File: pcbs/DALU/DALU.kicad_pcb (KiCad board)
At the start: 4 copper layers, 94 parts, among them J201 Conn_02x20_Odd_Even, U201 74HC245, U202 74HC245, U203 74HC245, U301 74HC138, U401 74HC86, U402 74HC08, U403 74HC86, U404 74HC86, U405 74HC283, U406 74HC283, U407 74HC245, U408 74HC245, U501 74HC00, U502 74HC00, U503 74HC245, U601 74HC86, U602 74HC86, U603 74HC245, U701 74HC32, U702 74HC32, U703 74HC245, U801 74HC74, U802 74HC32, U803 74HCT574, U901 74HC08, U902 74HC08, U903 74HC245

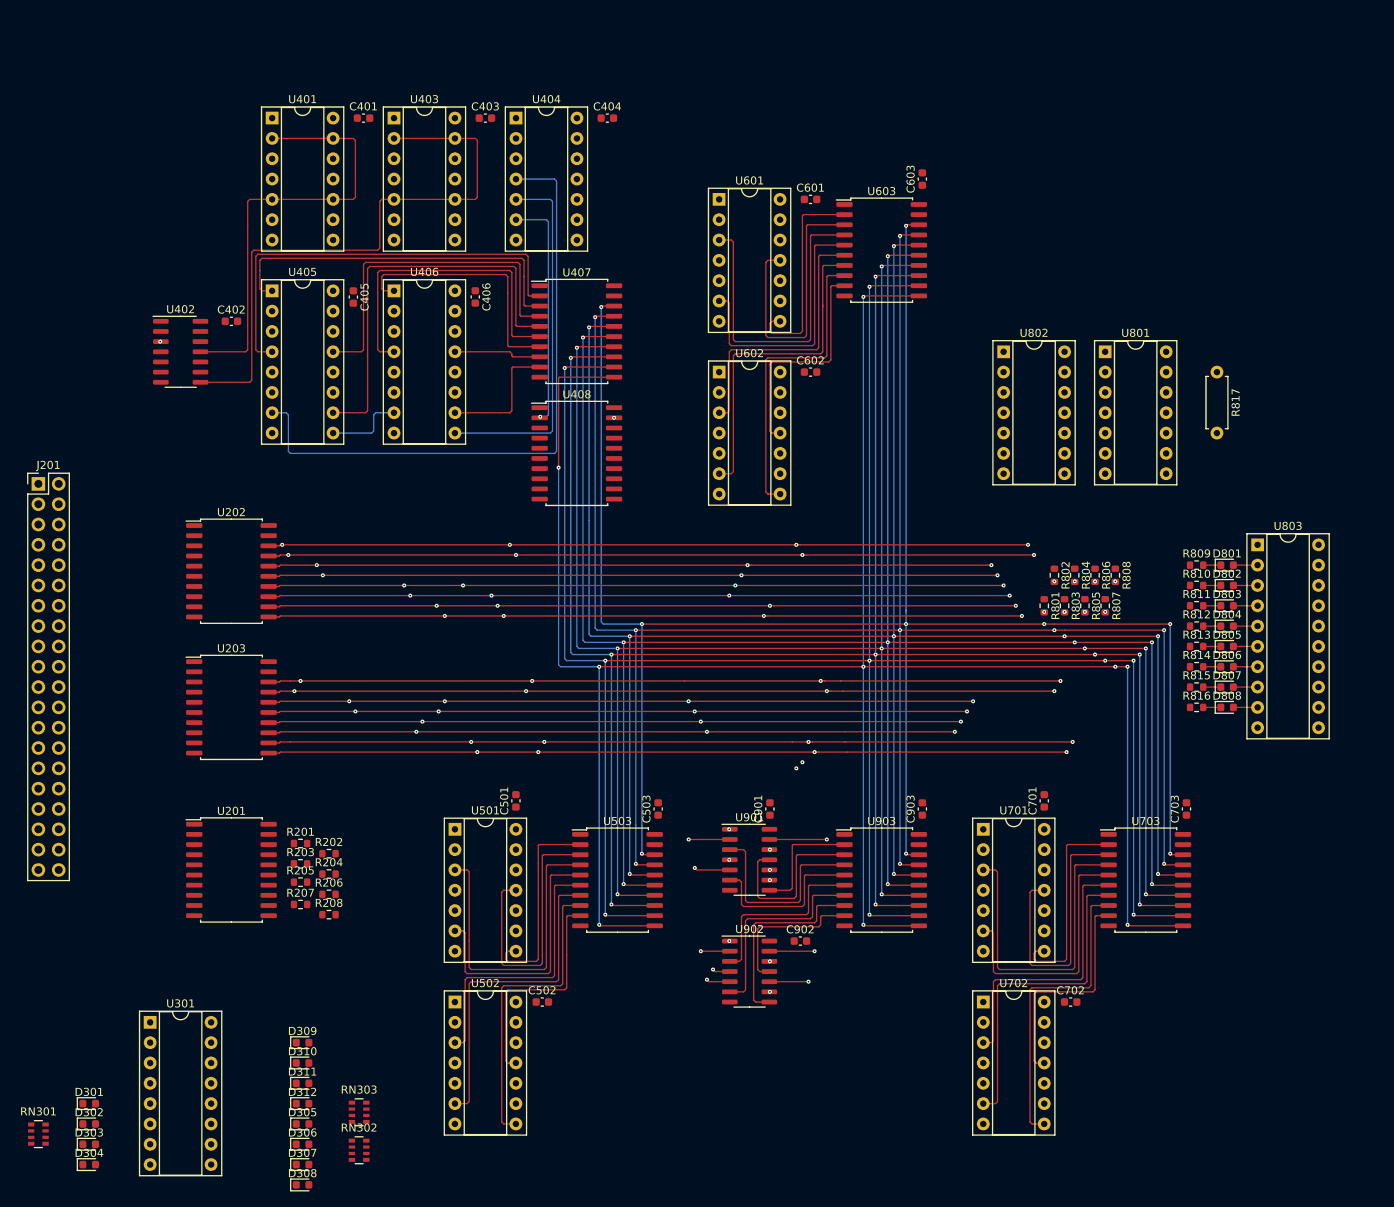
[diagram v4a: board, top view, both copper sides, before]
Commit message: Starting to connect up control wires
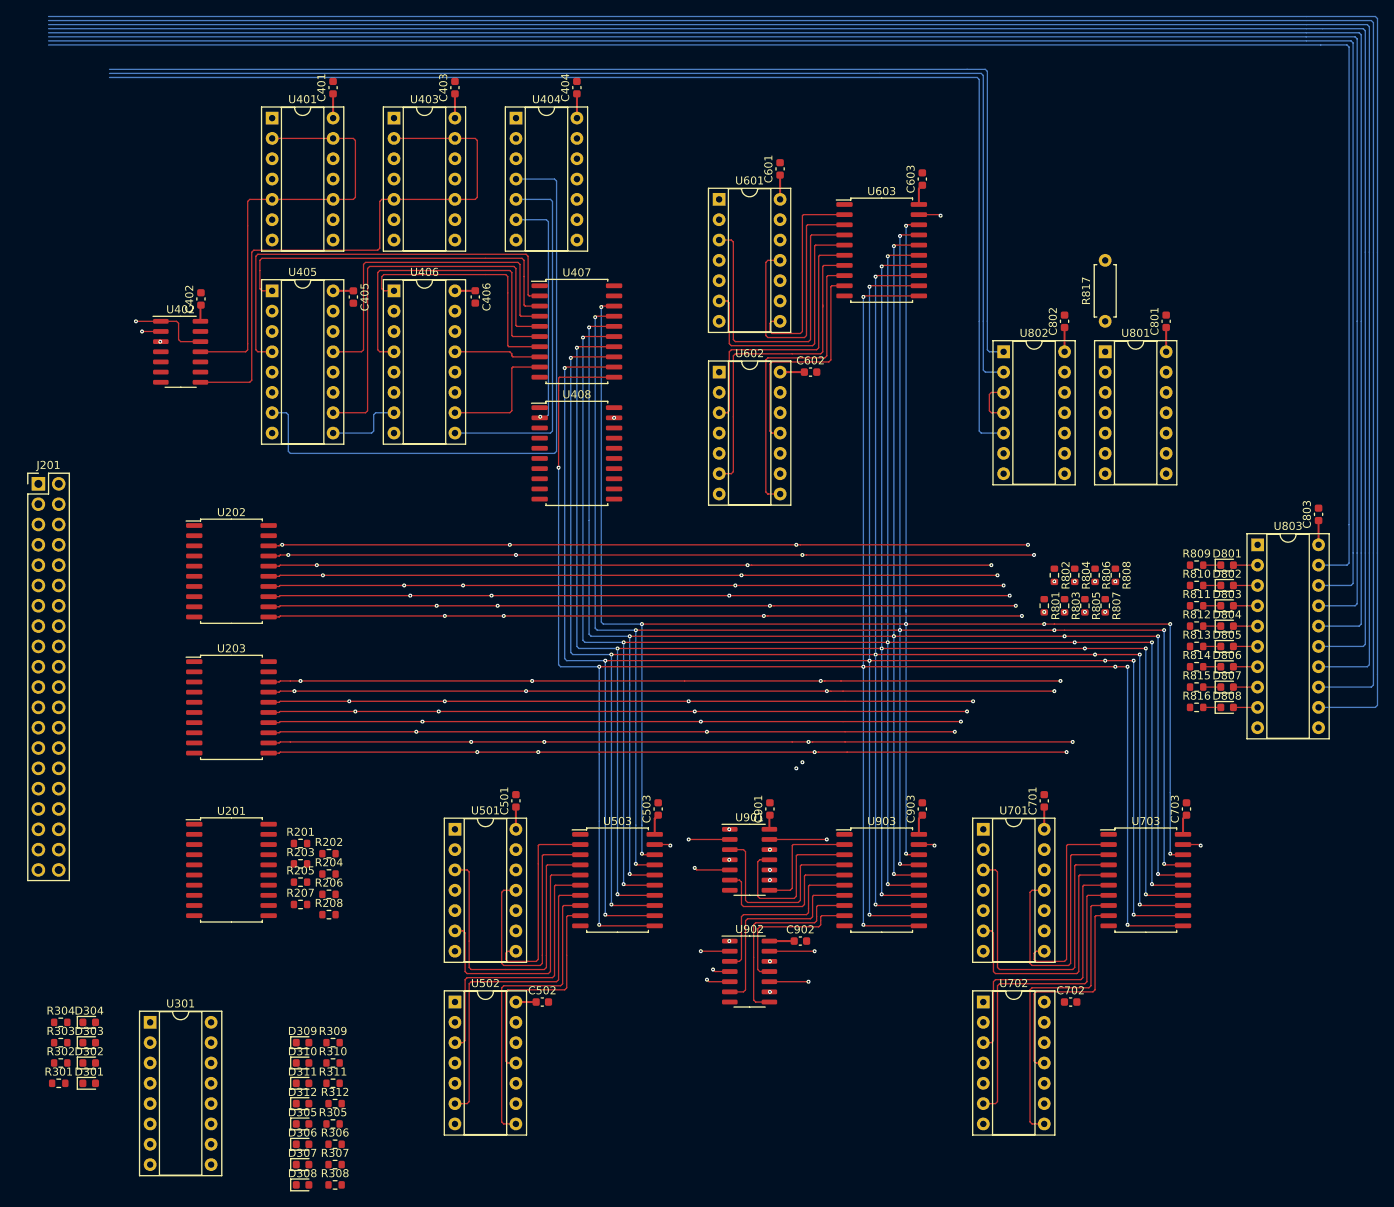
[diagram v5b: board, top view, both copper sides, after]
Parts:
- removed RN301, RN302, RN303: 4k7, Resistor_SMD:R_Array_Convex_4x0603
- added C801: 100n, Capacitor_SMD:C_0603_1608Metric, F.Cu at (175.3, 78.7)
- added C802: 100n, Capacitor_SMD:C_0603_1608Metric, F.Cu at (162.6, 78.7)
- added C803: 100n, Capacitor_SMD:C_0603_1608Metric, F.Cu at (194.3, 102.9)
- added R301: 4k7, Resistor_SMD:R_0603_1608Metric, F.Cu at (36.8, 174.0)
- added R302: 4k7, Resistor_SMD:R_0603_1608Metric, F.Cu at (37.1, 171.4)
- added R303: 4k7, Resistor_SMD:R_0603_1608Metric, F.Cu at (37.1, 168.9)
- added R304: 4k7, Resistor_SMD:R_0603_1608Metric, F.Cu at (37.1, 166.4)
- added R305: 4k7, Resistor_SMD:R_0603_1608Metric, F.Cu at (71.1, 179.1)
- added R306: 4k7, Resistor_SMD:R_0603_1608Metric, F.Cu at (71.4, 181.6)
- added R307: 4k7, Resistor_SMD:R_0603_1608Metric, F.Cu at (71.4, 184.2)
- added R308: 4k7, Resistor_SMD:R_0603_1608Metric, F.Cu at (71.4, 186.7)
- added R309: 4k7, Resistor_SMD:R_0603_1608Metric, F.Cu at (71.1, 168.9)
- added R310: 4k7, Resistor_SMD:R_0603_1608Metric, F.Cu at (71.1, 171.4)
- added R311: 4k7, Resistor_SMD:R_0603_1608Metric, F.Cu at (71.1, 174.0)
- added R312: 4k7, Resistor_SMD:R_0603_1608Metric, F.Cu at (71.4, 176.5)
- moved D304 17.8 mm to (40.6, 166.4)
- moved R817 15.3 mm to (167.6, 78.7), turned to 90 degrees
- moved D303 12.7 mm to (40.6, 168.9)
- moved D302 7.62 mm to (40.6, 171.4)
- moved C401 5.39 mm to (71.1, 49.5), turned to 90 degrees
- moved C403 5.39 mm to (86.4, 49.5), turned to 90 degrees
- moved C404 5.39 mm to (101.6, 49.5), turned to 90 degrees
- moved C601 5.39 mm to (127.0, 59.7), turned to 90 degrees
- moved C402 4.72 mm to (54.6, 75.9), turned to 90 degrees
- moved D301 2.54 mm to (40.6, 174.0)
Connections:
- U402 pad 1: /AdderSubtractor/~{ADD} -> /Decoder/~{ADD}
- U402 pad 12: /AdderSubtractor/~{ADD} -> /Decoder/~{ADD}
- U402 pad 2: /AdderSubtractor/~{SUBTRACT} -> /Decoder/~{SUBTRACT}
- U402 pad 9: /AdderSubtractor/~{ADD} -> /Decoder/~{ADD}
- U404 pad 4: /AdderSubtractor/~{ADD} -> /Decoder/~{ADD}
- U405 pad 7: /AdderSubtractor/~{ADD} -> /Decoder/~{ADD}
- U503 pad 19: /NAND/~{NAND} -> /Decoder/~{NAND}
- U603 pad 19: unconnected-(U603-Pad19) -> /Decoder/~{XOR}
- U703 pad 19: /OR/~{OR} -> /Decoder/~{OR}
- U802 pad 14: unconnected-(U802-Pad14) -> +5V
- U802 pad 7: unconnected-(U802-Pad7) -> GND
- U903 pad 19: /AND/~{AND} -> /Decoder/~{AND}
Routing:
- net /Output Stage/C7: track 0.00 -> 259.5 mm
- net /Output Stage/C6: track 0.00 -> 255.5 mm
- net /Output Stage/C5: track 0.00 -> 251.4 mm
- net /Output Stage/C4: track 0.00 -> 247.4 mm
- net /Output Stage/EXECUTE: track 0.00 -> 243.5 mm
- net /Output Stage/C3: track 0.00 -> 243.3 mm
- net /Output Stage/C2: track 0.00 -> 239.2 mm
- net /Output Stage/C1: track 0.00 -> 235.2 mm
- net /Output Stage/C0: track 0.00 -> 231.1 mm
- net /Decoder/~{XOR}: track 0.00 -> 221.8 mm, vias 0 -> 1
- net /Decoder/~{ADD}: track 0.00 -> 187.3 mm, vias 0 -> 1
- net /Decoder/~{OR}: track 0.00 -> 173.5 mm, vias 0 -> 1
- net /Output Stage/COMMIT: track 0.00 -> 155.9 mm
- net /Output Stage/DECODE: track 0.00 -> 146.8 mm
- net /Decoder/~{AND}: track 0.00 -> 143.3 mm, vias 0 -> 1
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
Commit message: Finish preliminary routing
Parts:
- added C201: 100n, Capacitor_SMD:C_0603_1608Metric, F.Cu at (66.3, 139.2)
- added C202: 100n, Capacitor_SMD:C_0603_1608Metric, F.Cu at (66.3, 104.4)
- added C203: 100n, Capacitor_SMD:C_0603_1608Metric, F.Cu at (66.3, 121.4)
- added C301: 100n, Capacitor_SMD:C_0603_1608Metric, F.Cu at (55.9, 162.6)
- added C407: 100n, Capacitor_SMD:C_0603_1608Metric, F.Cu at (109.5, 74.4)
- added C408: 100n, Capacitor_SMD:C_0603_1608Metric, F.Cu at (109.5, 89.7)
- moved R201 6.04 mm to (72.6, 141.7)
- moved R202 6.04 mm to (76.2, 143.0)
- moved R203 6.04 mm to (72.6, 144.3)
- moved R204 6.04 mm to (76.2, 145.5)
- moved R206 6.04 mm to (76.2, 148.1)
- moved R207 6.04 mm to (72.6, 149.4)
- moved R208 6.04 mm to (76.2, 150.6)
- moved R205 5.95 mm to (72.6, 146.8)
- moved U201 2.54 mm to (58.4, 144.8)
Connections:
- J201 pad 11: unconnected-(J201-Pad11) -> /Connector/C4
- J201 pad 13: unconnected-(J201-Pad13) -> /Connector/C5
- J201 pad 15: unconnected-(J201-Pad15) -> /Connector/C6
- J201 pad 17: unconnected-(J201-Pad17) -> /Connector/C7
- J201 pad 19: unconnected-(J201-Pad19) -> /Connector/DALUFLAG
- J201 pad 3: unconnected-(J201-Pad3) -> /Connector/C0
- J201 pad 5: unconnected-(J201-Pad5) -> /Connector/C1
- J201 pad 7: unconnected-(J201-Pad7) -> /Connector/C2
- J201 pad 9: unconnected-(J201-Pad9) -> /Connector/C3
- R817 pad 1: /Output Stage/FLAG -> /AdderSubtractor/FLAG
- U201 pad 1: unconnected-(U201-Pad1) -> +5V
- U201 pad 20: unconnected-(U201-Pad20) -> +5V
- U202 pad 20: unconnected-(U202-Pad20) -> +5V
- U203 pad 20: unconnected-(U203-Pad20) -> +5V
- U801 pad 2: /Output Stage/FLAG -> /AdderSubtractor/FLAG
- U801 pad 3: /Output Stage/EXECUTE -> /Connector/Control.Execute
- U801 pad 5: /Output Stage/DALUFLAG -> /Connector/DALUFLAG
- U802 pad 1: /Output Stage/DECODE -> /Connector/Control.Decode
- U802 pad 2: /Output Stage/EXECUTE -> /Connector/Control.Execute
- U802 pad 5: /Output Stage/COMMIT -> /Connector/Control.Commit
- U803 pad 11: /Output Stage/EXECUTE -> /Connector/Control.Execute
- U803 pad 12: /Output Stage/C7 -> /Connector/C7
- U803 pad 13: /Output Stage/C6 -> /Connector/C6
- U803 pad 14: /Output Stage/C5 -> /Connector/C5
- U803 pad 15: /Output Stage/C4 -> /Connector/C4
- U803 pad 16: /Output Stage/C3 -> /Connector/C3
- U803 pad 17: /Output Stage/C2 -> /Connector/C2
- U803 pad 18: /Output Stage/C1 -> /Connector/C1
- U803 pad 19: /Output Stage/C0 -> /Connector/C0
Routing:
- net /Connector/Control.Execute: track 0.00 -> 371.6 mm, vias 0 -> 1
- net /Connector/C7: track 0.00 -> 351.4 mm
- net /Connector/C6: track 0.00 -> 343.3 mm
- net /Connector/C5: track 0.00 -> 335.2 mm
- net /Connector/C4: track 0.00 -> 327.1 mm
- net /Connector/C3: track 0.00 -> 318.9 mm
- net /Connector/C2: track 0.00 -> 310.8 mm
- net /Connector/C1: track 0.00 -> 302.7 mm
- net /Connector/C0: track 0.00 -> 294.6 mm
- net /Connector/Control.Commit: track 0.00 -> 287.0 mm, vias 0 -> 1
- net /Connector/Control.Decode: track 0.00 -> 278.7 mm, vias 0 -> 1
- net /Connector/DALUFLAG: track 0.00 -> 276.8 mm
- net /Output Stage/C7: track 259.5 -> 0.00 mm
- net /Output Stage/C6: track 255.5 -> 0.00 mm
- net /Output Stage/C5: track 251.4 -> 0.00 mm
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
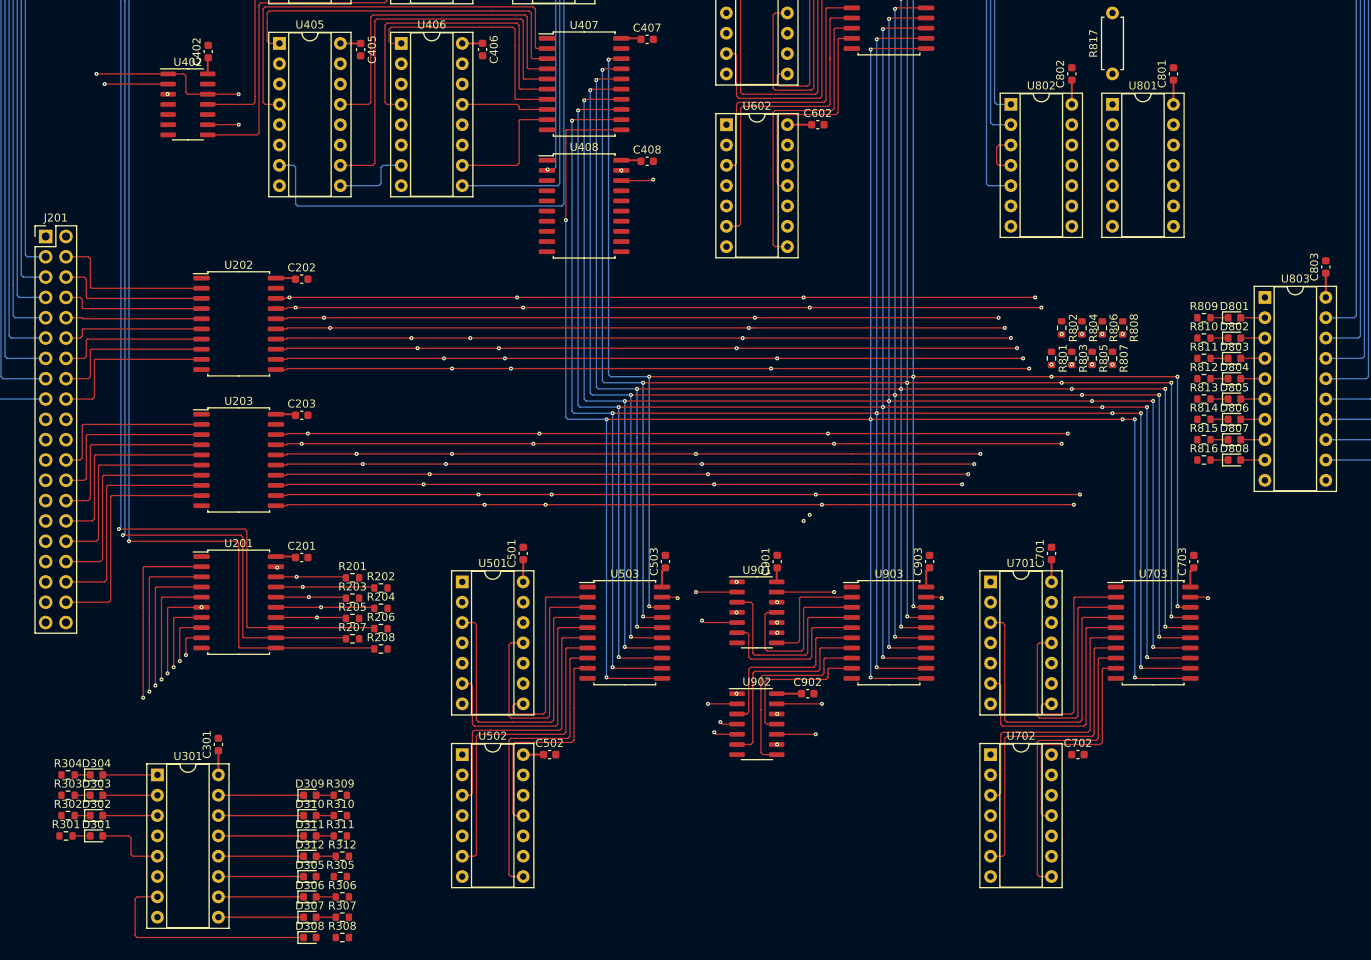
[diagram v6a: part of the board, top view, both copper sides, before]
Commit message: Forgot to invert the ORs in the output stage....
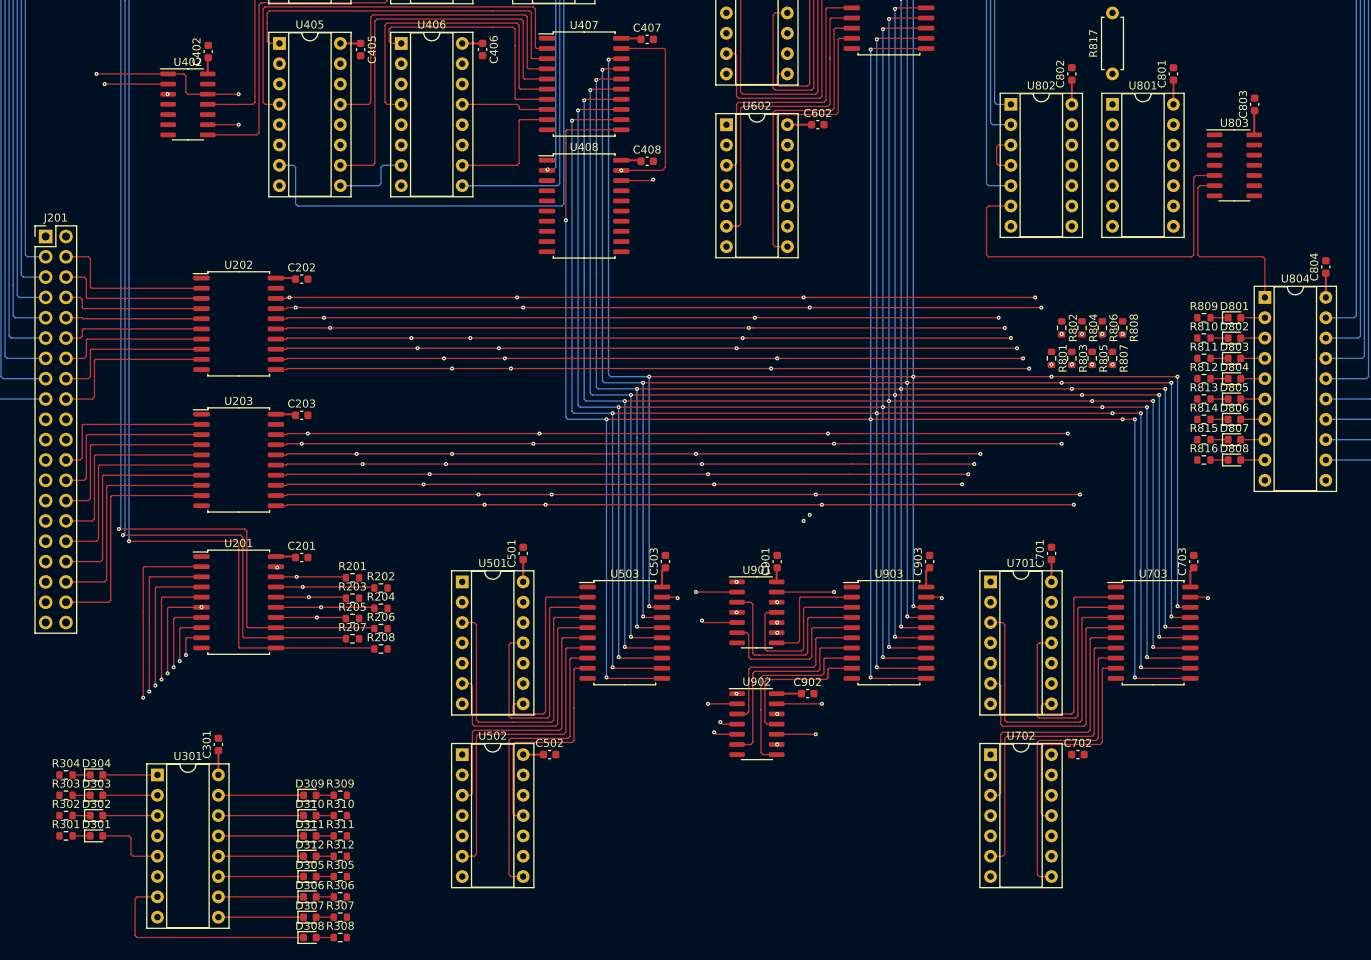
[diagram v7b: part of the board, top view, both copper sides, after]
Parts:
- added C804: 100n, Capacitor_SMD:C_0603_1608Metric, F.Cu at (194.3, 102.9)
- added U803: 74HC14, Package_SO:SOIC-14_3.9x8.7mm_P1.27mm, F.Cu at (182.9, 90.2)
- moved C803 22.2 mm to (185.4, 82.5)
- moved R302 0.25 mm to (36.8, 171.4)
- moved R303 0.25 mm to (36.8, 168.9)
- moved R304 0.25 mm to (36.8, 166.4)
- moved R306 0.25 mm to (71.1, 181.6)
- moved R307 0.25 mm to (71.1, 184.2)
- moved R308 0.25 mm to (71.1, 186.7)
- moved R312 0.25 mm to (71.1, 176.5)
- renumbered U803 to U804
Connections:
- U802 pad 6: /Output Stage/~{OE} -> Net-(U802-Pad6)
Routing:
- net Net-(U802-Pad6): track 0.00 -> 47.5 mm
- net /AdderSubtractor/~{OE}: track 75.6 -> 101.6 mm
- net /Output Stage/~{OE}: track 47.8 -> 24.0 mm
- net +5V: track 70.2 -> 73.3 mm
- net Net-(D308-Pad2): track 0.00 -> 2.20 mm
- net Net-(D305-Pad2): track 0.00 -> 2.20 mm
- net /AND/A4: track 307.2 -> 306.2 mm
